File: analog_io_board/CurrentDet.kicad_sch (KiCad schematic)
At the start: 20 parts, among them J3 DG141R-02, U7 LMV358IDT (SO-8)

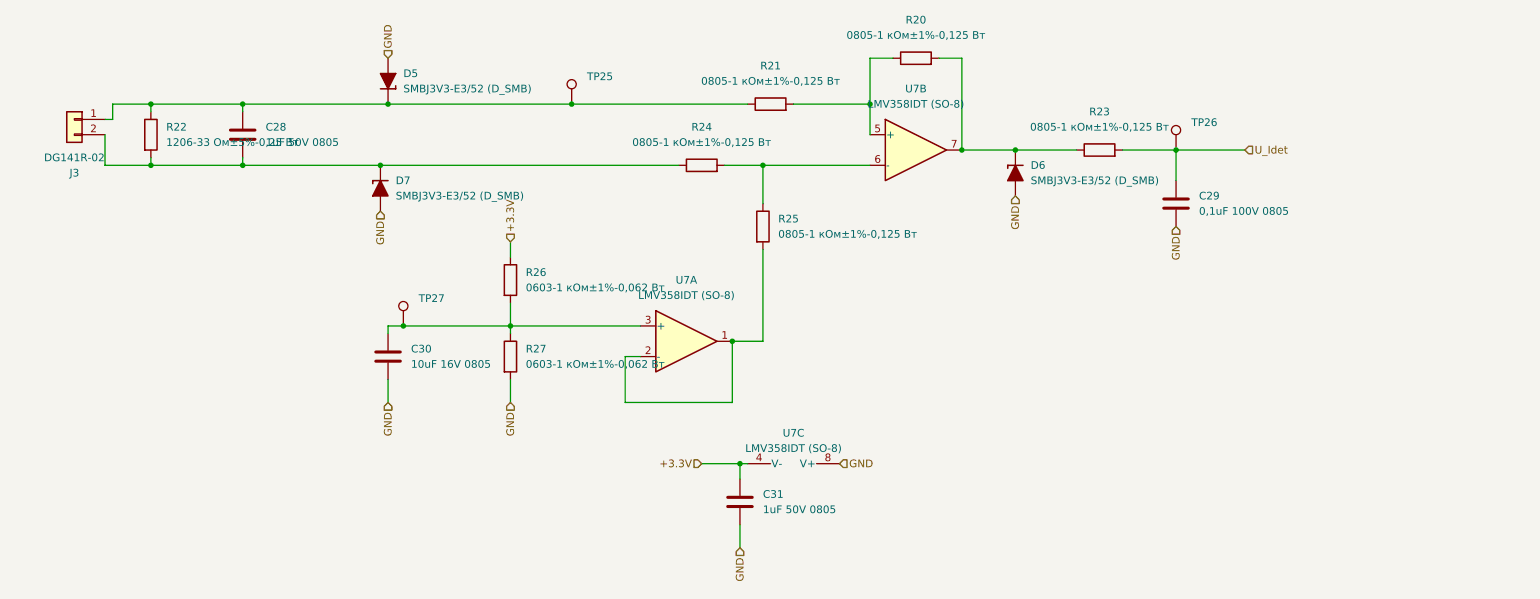
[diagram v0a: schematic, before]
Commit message: all замменил резисторы failsafe в плате контроллера и обрал из перечня во всех остальных
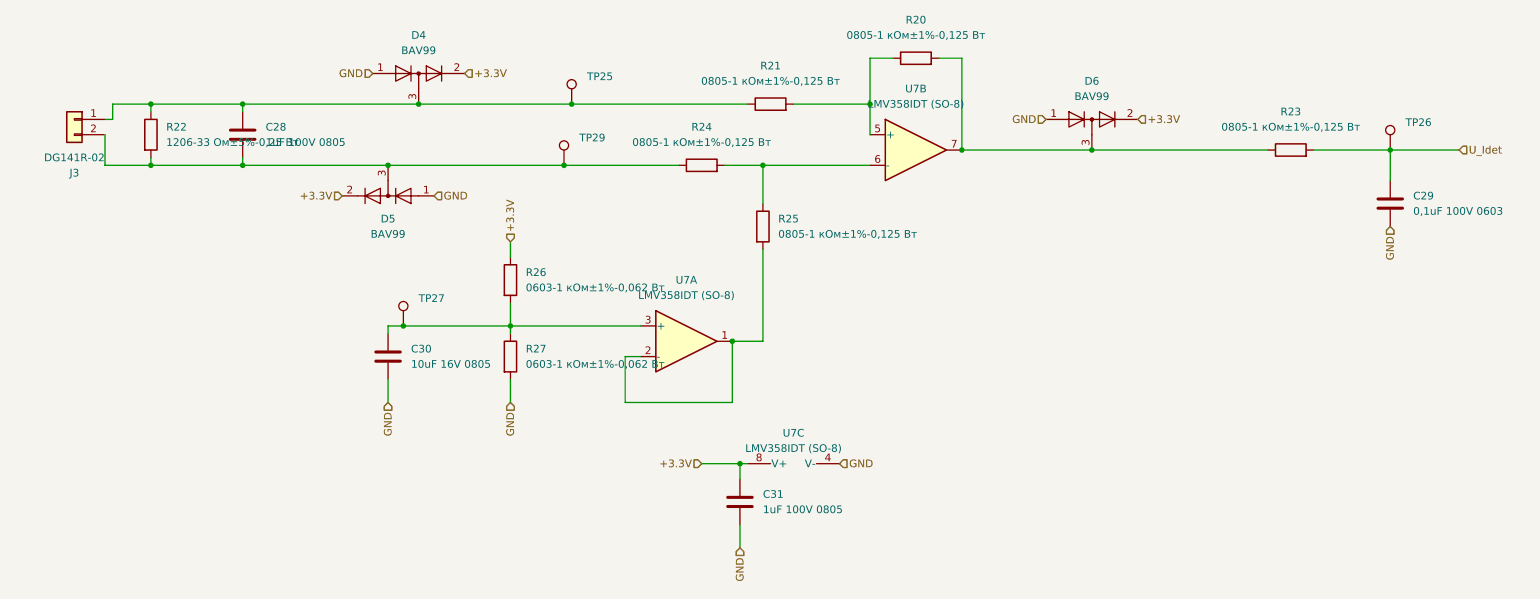
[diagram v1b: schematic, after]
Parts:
- removed D5, D6, D7: SMBJ3V3-E3/52 (D_SMB), Diode_SMD:D_SMB, symbol PCM_Diode_TVS_AKL:SMBJ5.0A
- added D4, D5, D6: BAV99, Package_TO_SOT_SMD:SOT-23, symbol Diode:BAV99
- added TP29: TestPoint, PCM_4ms_TestPoint:TestPoint_D1, symbol Connector:TestPoint
- C28, C31: value 1uF 50V 0805 -> 1uF 100V 0805
- C29: value 0,1uF 100V 0805 -> 0,1uF 100V 0603; footprint Capacitor_SMD:C_0805_2012Metric_Pad1.18x1.45mm_HandSolder -> Capacitor_SMD:C_0603_1608Metric_Pad1.08x0.95mm_HandSolder
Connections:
- net +3.3V: now also U7.8 (V+), D4.2 (A), D5.2 (A), D6.2 (A); no longer U7.4 (V-)
- net GND: now also U7.4 (V-), D4.1 (K), D5.1 (K), D6.1 (K); no longer U7.8 (V+)
- net at R20.2, R23.1, U7.7: now also D6.3 (K)
- net at C28.1, J3.1 (Pin_1), R21.1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: now also D4.3 (K)
- net at C28.2, J3.2 (Pin_2), R22.2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: now also D5.3 (K), TP29.1
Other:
- moved on the sheet: C29, R23, TP26, U7C

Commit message: analog board refresh
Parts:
- R22: renamed from R20; value 0805-1 кОм±1%-0,125 Вт -> 0805 510 Ом±1%-0,125 Вт
- R27: renamed from R25; value 0805-1 кОм±1%-0,125 Вт -> 0805 510 Ом±1%-0,125 Вт
- renumbered D4 to D3, D6 to D4, J3 to J7, R21 to R23, R22 to R24, R23 to R25, R24 to R26, R26 to R28, R27 to R29, TP25 to TP23, TP26 to TP24, TP29 to TP25, TP27 to TP26, U7 to U9
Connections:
- net at R22.1, R23.2: now also U9.6 (-); no longer U9.5 (+)
- net at R26.2, R27.1: now also U9.5 (+); no longer U9.6 (-)

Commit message: analog board refresh pcb
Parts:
- C28, C31: footprint Capacitor_SMD:C_0805_2012Metric_Pad1.18x1.45mm_HandSolder -> Capacitor_SMD:C_0805_2012Metric
- C29: footprint Capacitor_SMD:C_0603_1608Metric_Pad1.08x0.95mm_HandSolder -> Capacitor_SMD:C_0603_1608Metric
- J5: renamed from J7; value DG141R-02 -> DG141R-2.54-02P
- R22, R23, R25, R26, R27: footprint Resistor_SMD:R_0805_2012Metric_Pad1.20x1.40mm_HandSolder -> Resistor_SMD:R_0805_2012Metric
- R28, R29: footprint Resistor_SMD:R_0603_1608Metric_Pad0.98x0.95mm_HandSolder -> Resistor_SMD:R_0603_1608Metric
- TP23, TP24, TP25, TP26: footprint PCM_4ms_TestPoint:TestPoint_D1 -> TestPoint:TestPoint_Pad_D1.0mm
- U9: footprint PCM_Package_SO_AKL:SO-8_3.9x4.9mm_P1.27mm -> Package_SO:SO-8_3.9x4.9mm_P1.27mm
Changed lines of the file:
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@@
 			)
 		)
-		(property "Description" ""
+		(property "Description" "BAV99 High-speed switching diodes, SOT-23"
 			(at 80.01 85.09 0)
 			(effects
@@
 			)
 		)
-		(property "Footprint" "Resistor_SMD:R_0603_1608Metric_Pad0.98x0.95mm_HandSolder"
+		(property "Footprint" "Resistor_SMD:R_0603_1608Metric"
 			(at 93.472 132.08 90)
 			(effects
@@
 			)
 		)
-		(property "Description" ""
+		(property "Description" "Resistor"
 			(at 95.25 132.08 0)
 			(effects
@@
 			)
 		)
-		(property "Footprint" "PCM_4ms_TestPoint:TestPoint_D1"
+		(property "Footprint" "TestPoint:TestPoint_Pad_D1.0mm"
 			(at 246.38 97.79 0)
 			(effects
@@
 			)
 		)
-		(property "Description" ""
+		(property "Description" "test point"
 			(at 241.3 97.79 0)
 			(effects
@@
 			)
 		)
-		(property "Footprint" "PCM_4ms_TestPoint:TestPoint_D1"
+		(property "Footprint" "TestPoint:TestPoint_Pad_D1.0mm"
 			(at 109.22 100.33 0)
 			(effects
@@
 			)
 		)
-		(property "Description" ""
+		(property "Description" "test point"
 			(at 104.14 100.33 0)
 			(effects
@@
 			)
 		)
-		(property "Description" ""
+		(property "Description" "BAV99 High-speed switching diodes, SOT-23"
 			(at 74.93 105.41 0)
 			(effects
@@
 			)
 		)
-		(property "Description" ""
+		(property "Description" "BAV99 High-speed switching diodes, SOT-23"
 			(at 191.77 92.71 0)
 			(effects
@@
 			)
 		)
-		(property "Footprint" "PCM_Package_SO_AKL:SO-8_3.9x4.9mm_P1.27mm"
+		(property "Footprint" "Package_SO:SO-8_3.9x4.9mm_P1.27mm"
 			(at 124.46 129.54 0)
 			(effects
@@
 			)
 		)
-		(property "Description" ""
+		(property "Description" "Dual Low-Voltage Rail-to-Rail Output Operational Amplifiers, SOIC-8/SSOP-8"
 			(at 124.46 129.54 0)
 			(effects
@@
 			)
 		)
-		(property "Footprint" "Resistor_SMD:R_0805_2012Metric_Pad1.20x1.40mm_HandSolder"
+		(property "Footprint" "Resistor_SMD:R_0805_2012Metric"
 			(at 224.79 99.568 90)
 			(effects
@@
 			)
 		)
-		(property "Description" ""
+		(property "Description" "Resistor"
 			(at 224.79 97.79 0)
 			(effects
@@
 			)
 		)
-		(property "Footprint" "PCM_4ms_TestPoint:TestPoint_D1"
+		(property "Footprint" "TestPoint:TestPoint_Pad_D1.0mm"
 			(at 82.55 127 0)
 			(effects
@@
 			)
 		)
-		(property "Description" ""
+		(property "Description" "test point"
 			(at 77.47 127 0)
 			(effects
@@
 		(on_board yes)
 		(dnp no)
-		(property "Reference" "J7"
+		(property "Reference" "J5"
 			(at 22.86 101.6 0)
 			(effects
@@
 			)
 		)
-		(property "Value" "DG141R-02"
+		(property "Value" "DG141R-2.54-02P"
 			(at 22.86 99.06 0)
 			(effects
@@
 			)
 		)
-		(property "Description" ""
+		(property "Description" "Generic connector, single row, 01x02, script generated (kicad-library-utils/schlib/autogen/connector/)"
 			(at 22.86 92.71 0)
 			(effects
@@
 			(project "analog_io_board"
 				(path "/c658a069-2acb-41ac-8530-c56b14d342d1/c60a24f7-547e-4015-b7ed-3ac264249d3c/e5a0086d-c448-49f4-b3f8-34e98e7dad54"
-					(reference "J7")
+					(reference "J5")
 					(unit 1)
 				)
@@
 			)
 		)
-		(property "Footprint" "Resistor_SMD:R_0805_2012Metric_Pad1.20x1.40mm_HandSolder"
+		(property "Footprint" "Resistor_SMD:R_0805_2012Metric"
 			(at 138.43 91.948 90)
 			(effects
@@
 			)
 		)
-		(property "Description" ""
+		(property "Description" "Resistor"
 			(at 138.43 90.17 0)
 			(effects
@@
 			)
 		)
-		(property "Footprint" "Resistor_SMD:R_0805_2012Metric_Pad1.20x1.40mm_HandSolder"
+		(property "Footprint" "Resistor_SMD:R_0805_2012Metric"
 			(at 162.56 84.328 90)
 			(effects
@@
 			)
 		)
-		(property "Description" ""
+		(property "Description" "Resistor"
 			(at 162.56 82.55 0)
 			(effects
@@
 			)
 		)
-		(property "Description" ""
+		(property "Description" "Unpolarized capacitor"
 			(at 74.93 132.08 0)
 			(effects
@@
 			)
 		)
-		(property "Footprint" "Capacitor_SMD:C_0603_1608Metric_Pad1.08x0.95mm_HandSolder"
+		(property "Footprint" "Capacitor_SMD:C_0603_1608Metric"
 			(at 242.2652 110.49 0)
 			(effects
@@
 			)
 		)
-		(property "Description" ""
+		(property "Description" "Unpolarized capacitor"
 			(at 241.3 106.68 0)
 			(effects
@@
 			)
 		)
-		(property "Footprint" "PCM_Package_SO_AKL:SO-8_3.9x4.9mm_P1.27mm"
+		(property "Footprint" "Package_SO:SO-8_3.9x4.9mm_P1.27mm"
 			(at 142.24 147.32 0)
 			(effects
@@
 			)
 		)
-		(property "Description" ""
+		(property "Description" "Dual Low-Voltage Rail-to-Rail Output Operational Amplifiers, SOIC-8/SSOP-8"
 			(at 142.24 147.32 0)
 			(effects
@@
 			)
 		)
-		(property "Footprint" "Resistor_SMD:R_0805_2012Metric_Pad1.20x1.40mm_HandSolder"
+		(property "Footprint" "Resistor_SMD:R_0805_2012Metric"
 			(at 135.382 110.49 90)
 			(effects
@@
 			)
 		)
-		(property "Description" ""
+		(property "Description" "Resistor"
 			(at 137.16 110.49 0)
 			(effects
@@
 			)
 		)
-		(property "Footprint" "PCM_4ms_TestPoint:TestPoint_D1"
+		(property "Footprint" "TestPoint:TestPoint_Pad_D1.0mm"
 			(at 110.49 90.17 0)
 			(effects
@@
 			)
 		)
-		(property "Description" ""
+		(property "Description" "test point"
 			(at 105.41 90.17 0)
 			(effects
@@
 			)
 		)
-		(property "Footprint" "Capacitor_SMD:C_0805_2012Metric_Pad1.18x1.45mm_HandSolder"
+		(property "Footprint" "Capacitor_SMD:C_0805_2012Metric"
 			(at 51.7652 99.06 0)
 			(effects
@@
 			)
 		)
-		(property "Description" ""
+		(property "Description" "Unpolarized capacitor"
 			(at 50.8 95.25 0)
 			(effects
@@
 			)
 		)
-		(property "Description" ""
+		(property "Description" "Resistor"
 			(at 35.56 95.25 0)
 			(effects
@@
 			)
 		)
-		(property "Footprint" "PCM_Package_SO_AKL:SO-8_3.9x4.9mm_P1.27mm"
+		(property "Footprint" "Package_SO:SO-8_3.9x4.9mm_P1.27mm"
 			(at 162.56 97.79 0)
 			(effects
@@
 			)
 		)
-		(property "Description" ""
+		(property "Description" "Dual Low-Voltage Rail-to-Rail Output Operational Amplifiers, SOIC-8/SSOP-8"
 			(at 162.56 97.79 0)
 			(effects
@@
 			)
 		)
-		(property "Footprint" "Resistor_SMD:R_0603_1608Metric_Pad0.98x0.95mm_HandSolder"
+		(property "Footprint" "Resistor_SMD:R_0603_1608Metric"
 			(at 93.472 119.38 90)
 			(effects
@@
 			)
 		)
-		(property "Description" ""
+		(property "Description" "Resistor"
 			(at 95.25 119.38 0)
 			(effects
@@
 			)
 		)
-		(property "Footprint" "Capacitor_SMD:C_0805_2012Metric_Pad1.18x1.45mm_HandSolder"
+		(property "Footprint" "Capacitor_SMD:C_0805_2012Metric"
 			(at 134.3152 160.02 0)
 			(effects
@@
 			)
 		)
-		(property "Description" ""
+		(property "Description" "Unpolarized capacitor"
 			(at 133.35 156.21 0)
 			(effects
@@
 			)
 		)
-		(property "Footprint" "Resistor_SMD:R_0805_2012Metric_Pad1.20x1.40mm_HandSolder"
+		(property "Footprint" "Resistor_SMD:R_0805_2012Metric"
 			(at 127 102.108 90)
 			(effects
@@
 			)
 		)
-		(property "Description" ""
+		(property "Description" "Resistor"
 			(at 127 100.33 0)
 			(effects

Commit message: update schemas
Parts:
- D3, D4, D5: value BAV99 -> BAV99 (SOT-23)
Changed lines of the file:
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@@
 			)
 		)
-		(property "Value" "BAV99"
+		(property "Value" "BAV99 (SOT-23)"
 			(at 80.01 81.28 0)
 			(effects
@@
 			)
 		)
-		(property "Value" "BAV99"
+		(property "Value" "BAV99 (SOT-23)"
 			(at 74.93 111.76 0)
 			(effects
@@
 			)
 		)
-		(property "Value" "BAV99"
+		(property "Value" "BAV99 (SOT-23)"
 			(at 191.77 88.9 0)
 			(effects
